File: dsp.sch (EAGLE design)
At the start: 131 parts, among them IC1 OPA2134P, IC2 OPA2134P, IC3 OPA2134P, U1 STM32F405RGT6, U2 CODECODER-WM8731SEDS/V(SSOP28), U4 LM2575HVS-3.3/NOPB, X1 ABLS-8.000MHZ-B4-T

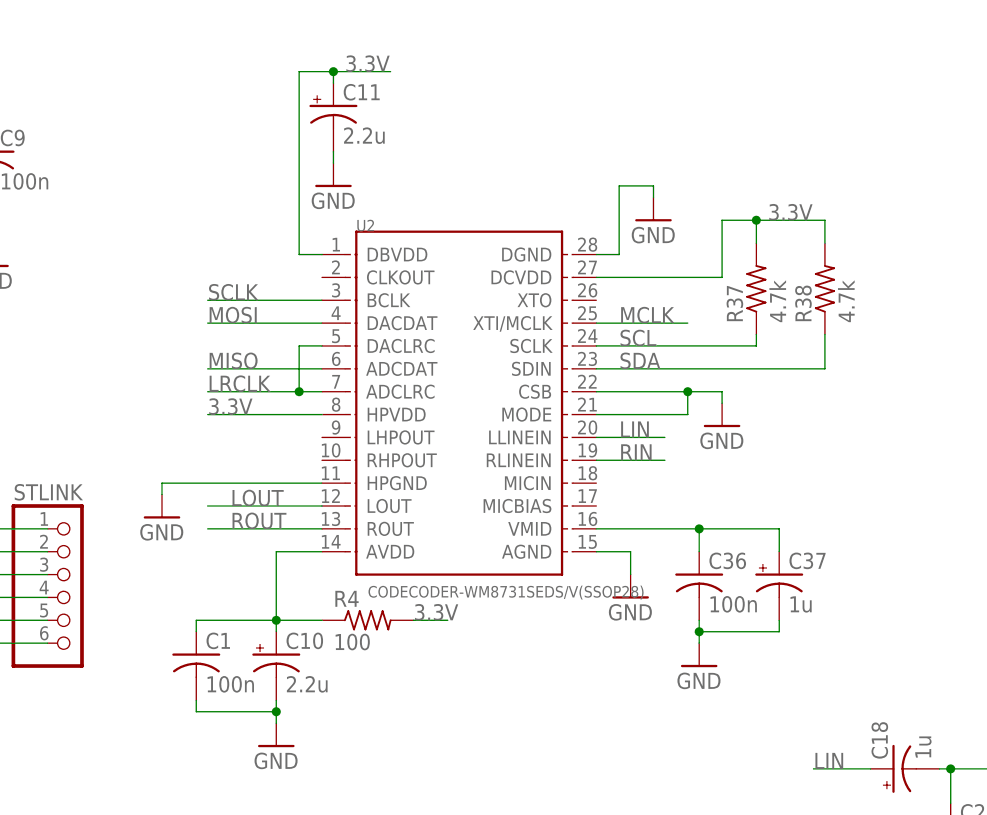
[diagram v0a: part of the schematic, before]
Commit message: fixed grounds problem on codec (post fab)
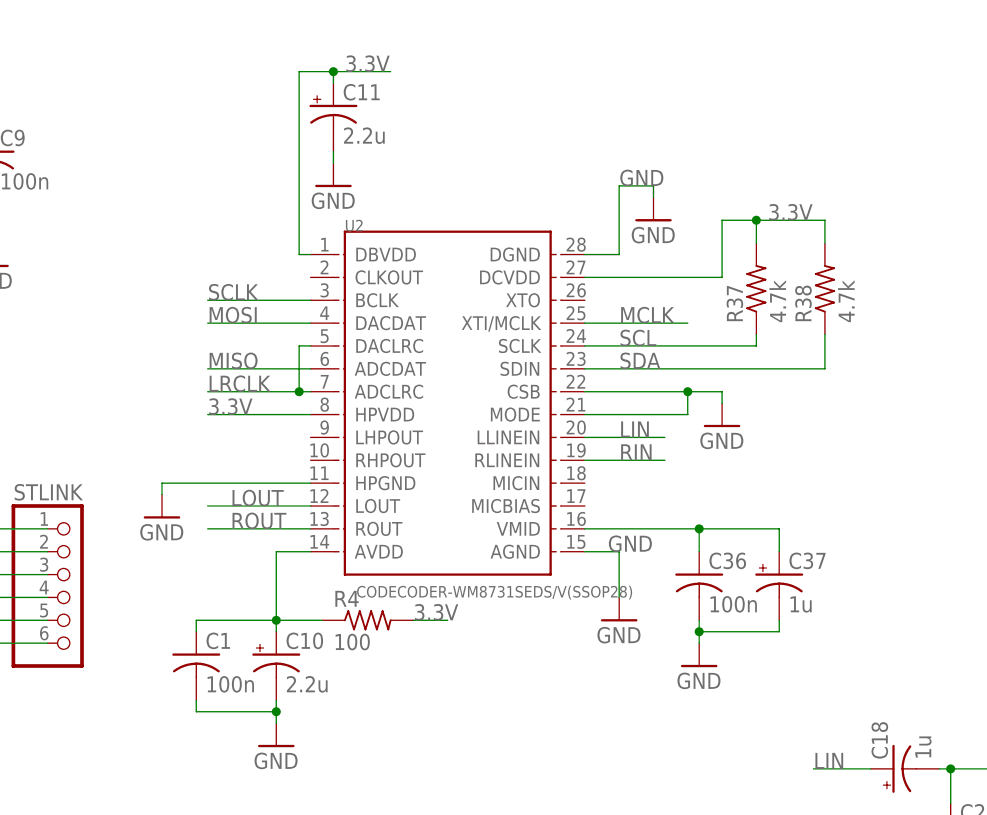
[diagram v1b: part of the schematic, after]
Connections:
- removed net AGND: U2.AGND
- removed net DGND: U2.DGND
- net GND: now also U2.AGND, U2.DGND
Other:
- moved on the sheet: U2

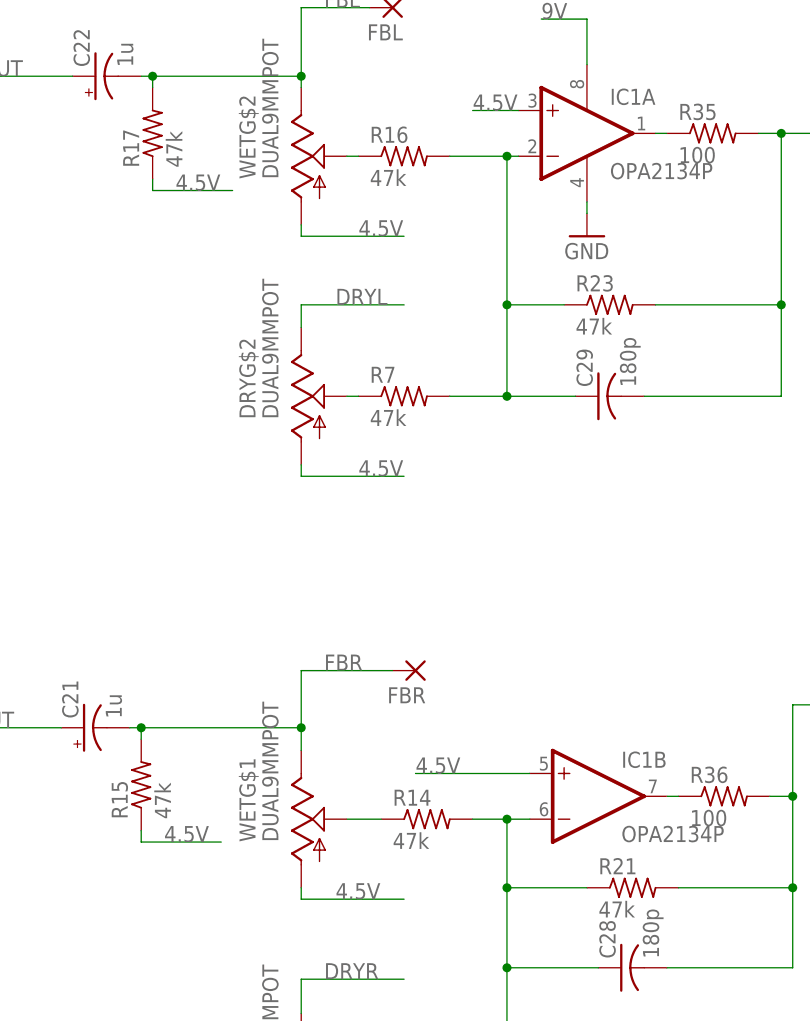
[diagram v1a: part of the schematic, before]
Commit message: updated mixer resistors for higher wet amplitude
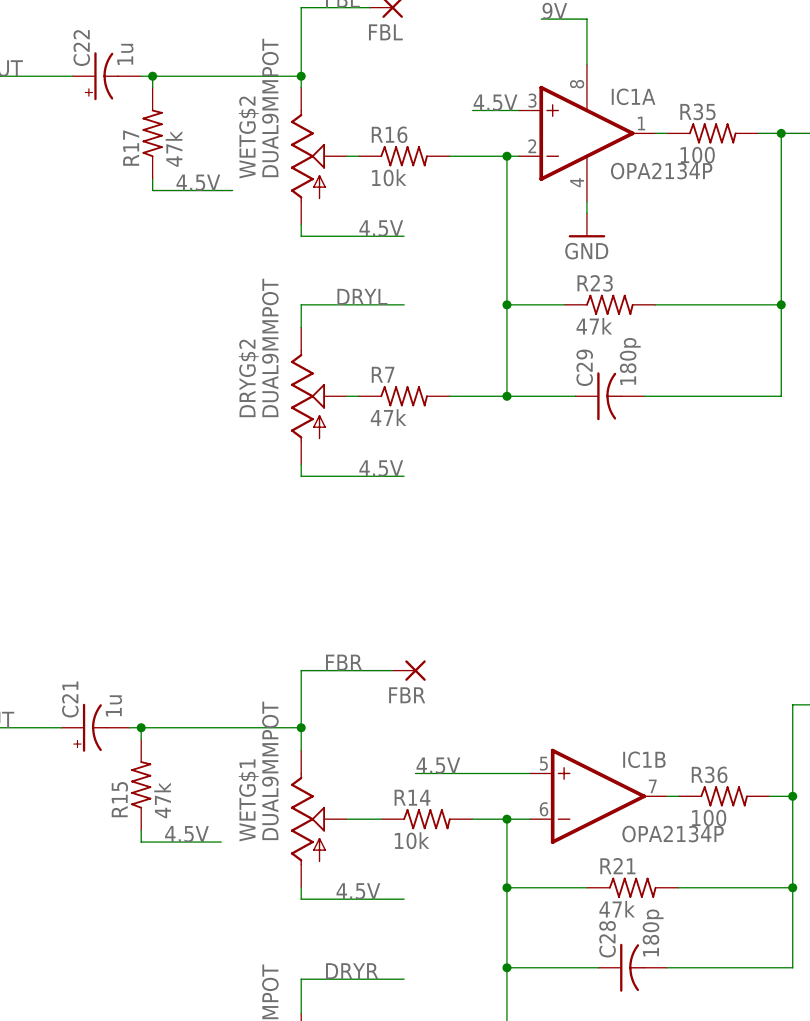
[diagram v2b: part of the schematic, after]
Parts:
- R14, R16: value 47k -> 10k
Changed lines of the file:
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@@
 <part name="C20" library="dan" deviceset="C-US" device="050-025X075" value="220p"/>
 <part name="C21" library="dan" deviceset="CPOL-US" device="E2.5-7" value="1u"/>
-<part name="R14" library="dan" deviceset="R-US_" device="0309/V" value="47k"/>
+<part name="R14" library="dan" deviceset="R-US_" device="0309/V" value="10k"/>
 <part name="R15" library="dan" deviceset="R-US_" device="0309/V" value="47k"/>
 <part name="C22" library="dan" deviceset="CPOL-US" device="E2.5-7" value="1u"/>
-<part name="R16" library="dan" deviceset="R-US_" device="0309/V" value="47k"/>
+<part name="R16" library="dan" deviceset="R-US_" device="0309/V" value="10k"/>
 <part name="R17" library="dan" deviceset="R-US_" device="0309/V" value="47k"/>
 <part name="IC1" library="dan" deviceset="OPA2134" device="P"/>
